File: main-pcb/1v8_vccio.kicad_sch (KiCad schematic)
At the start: 1 part, among them U1 XC7S100-1FGGA484C

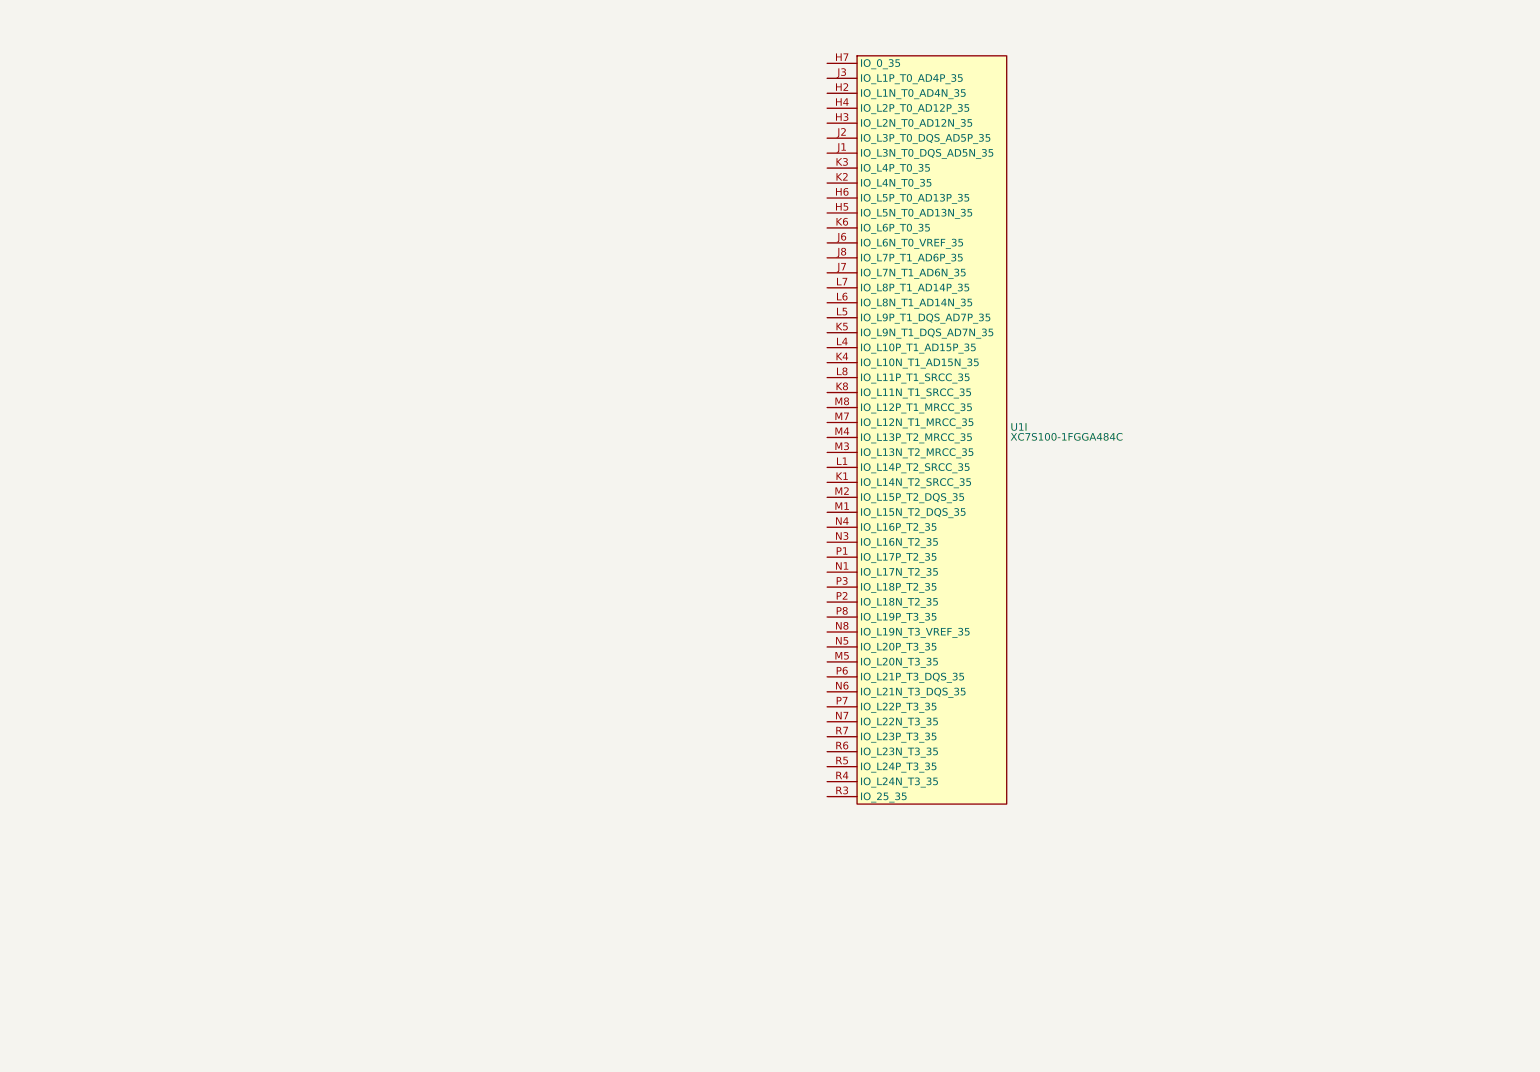
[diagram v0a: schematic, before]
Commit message: Initial design mostly done aside from USB connector, review, test points
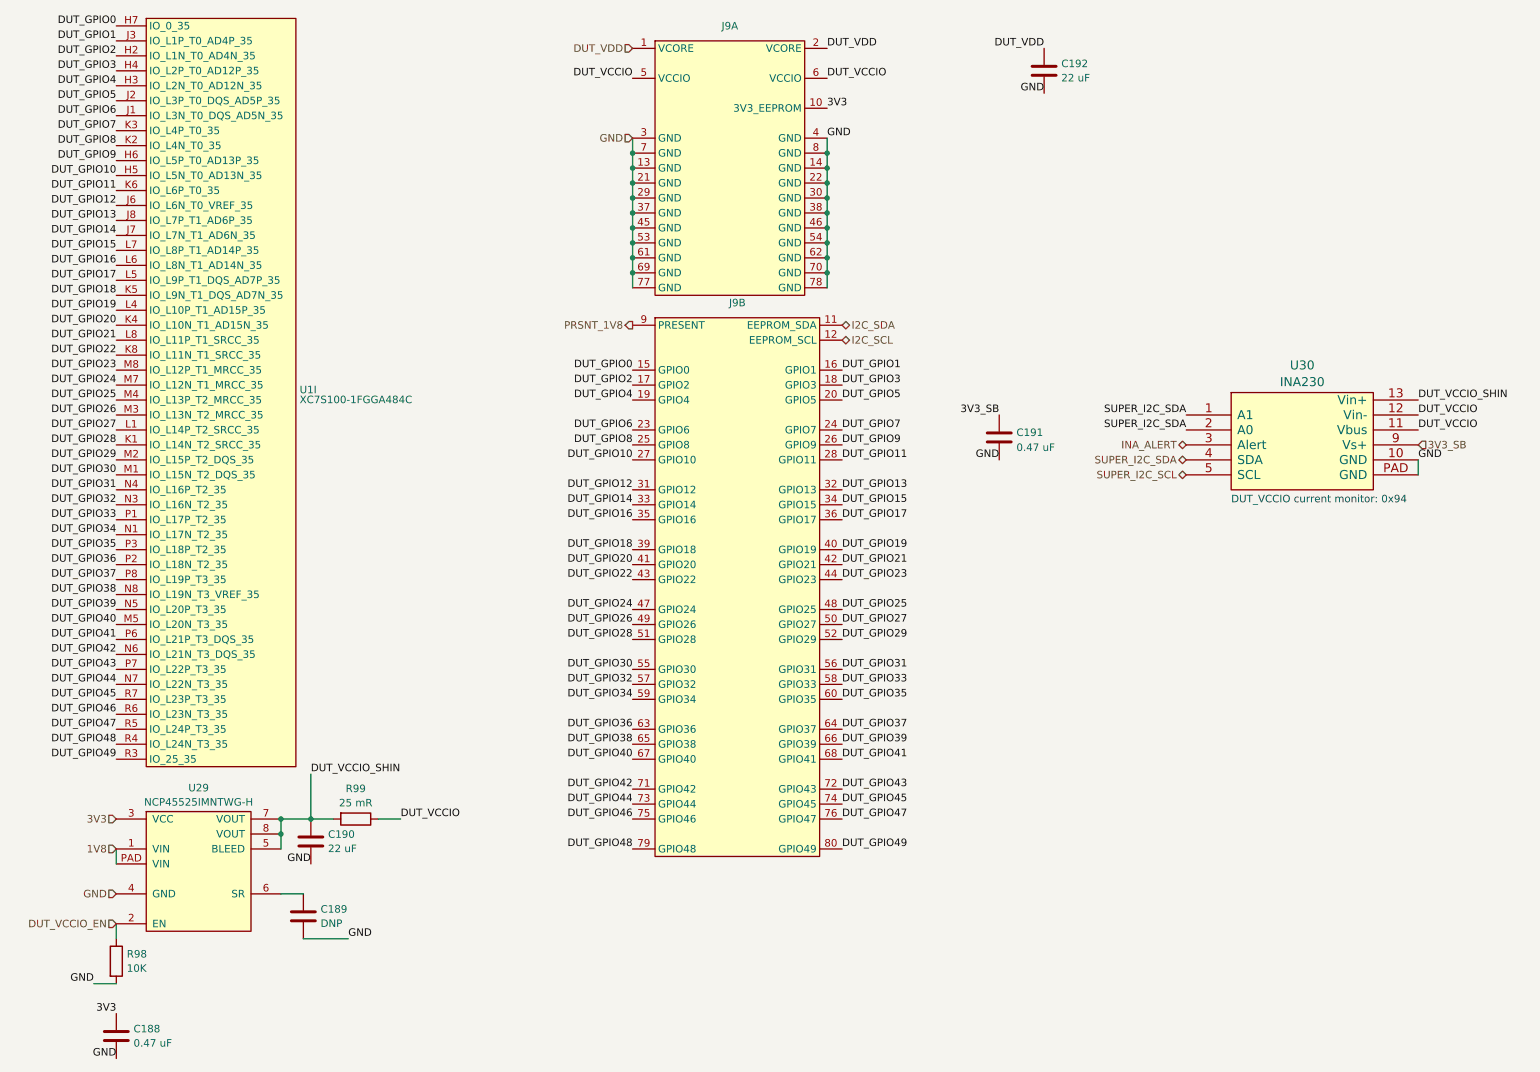
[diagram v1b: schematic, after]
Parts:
- added C188: 0.47 uF, symbol device:C
- added C189: DNP, symbol device:C
- added C190, C192: 22 uF, symbol device:C
- added C191: 0.47 uF, azonenberg_pcb:EIA_0402_CAP_NOSILK, symbol device:C
- added J9: ~, symbol special-azonenberg:CONN_DUMPTRUCK_HOST
- added R98: 10K, symbol device:R
- added R99: 25 mR, symbol passive-azonenberg:R_PWR
- added U29: NCP45525IMNTWG-H, symbol power-azonenberg:NCP45525
- added U30: INA230, azonenberg_pcb:QFN_16_0.5MM_3x3MM, symbol special-azonenberg:INA230
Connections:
- net DUT_GPIO2: now reaches U1.H2 (IO_L1N_T0_AD4N_35)
- net DUT_GPIO2: now also J9.17 (GPIO2)
- net DUT_GPIO4: now reaches U1.H3 (IO_L2N_T0_AD12N_35)
- net DUT_GPIO4: now also J9.19 (GPIO4)
- net DUT_GPIO3: now reaches U1.H4 (IO_L2P_T0_AD12P_35)
- net DUT_GPIO3: now also J9.18 (GPIO3)
- net DUT_GPIO10: now reaches U1.H5 (IO_L5N_T0_AD13N_35)
- net DUT_GPIO10: now also J9.27 (GPIO10)
- net DUT_GPIO9: now reaches U1.H6 (IO_L5P_T0_AD13P_35)
- net DUT_GPIO9: now also J9.26 (GPIO9)
- net DUT_GPIO0: now reaches U1.H7 (IO_0_35)
- net DUT_GPIO0: now also J9.15 (GPIO0)
- net DUT_GPIO6: now reaches U1.J1 (IO_L3N_T0_DQS_AD5N_35)
- net DUT_GPIO6: now also J9.23 (GPIO6)
- net DUT_GPIO5: now reaches U1.J2 (IO_L3P_T0_DQS_AD5P_35)
- net DUT_GPIO5: now also J9.20 (GPIO5)
- net DUT_GPIO1: now reaches U1.J3 (IO_L1P_T0_AD4P_35)
- net DUT_GPIO1: now also J9.16 (GPIO1)
- net DUT_GPIO12: now reaches U1.J6 (IO_L6N_T0_VREF_35)
- net DUT_GPIO12: now also J9.31 (GPIO12)
- net DUT_GPIO14: now reaches U1.J7 (IO_L7N_T1_AD6N_35)
- net DUT_GPIO14: now also J9.33 (GPIO14)
- net DUT_GPIO13: now reaches U1.J8 (IO_L7P_T1_AD6P_35)
- net DUT_GPIO13: now also J9.32 (GPIO13)
- net DUT_GPIO28: now reaches U1.K1 (IO_L14N_T2_SRCC_35)
- net DUT_GPIO28: now also J9.51 (GPIO28)
- net DUT_GPIO8: now reaches U1.K2 (IO_L4N_T0_35)
- net DUT_GPIO8: now also J9.25 (GPIO8)
- net DUT_GPIO7: now reaches U1.K3 (IO_L4P_T0_35)
- net DUT_GPIO7: now also J9.24 (GPIO7)
- net DUT_GPIO20: now reaches U1.K4 (IO_L10N_T1_AD15N_35)
- net DUT_GPIO20: now also J9.41 (GPIO20)
- net DUT_GPIO18: now reaches U1.K5 (IO_L9N_T1_DQS_AD7N_35)
- net DUT_GPIO18: now also J9.39 (GPIO18)
- net DUT_GPIO11: now reaches U1.K6 (IO_L6P_T0_35)
- net DUT_GPIO11: now also J9.28 (GPIO11)
- net DUT_GPIO22: now reaches U1.K8 (IO_L11N_T1_SRCC_35)
- net DUT_GPIO22: now also J9.43 (GPIO22)
- net DUT_GPIO27: now reaches U1.L1 (IO_L14P_T2_SRCC_35)
- net DUT_GPIO27: now also J9.50 (GPIO27)
- net DUT_GPIO19: now reaches U1.L4 (IO_L10P_T1_AD15P_35)
- net DUT_GPIO19: now also J9.40 (GPIO19)
- net DUT_GPIO17: now reaches U1.L5 (IO_L9P_T1_DQS_AD7P_35)
- net DUT_GPIO17: now also J9.36 (GPIO17)
- net DUT_GPIO16: now reaches U1.L6 (IO_L8N_T1_AD14N_35)
- net DUT_GPIO16: now also J9.35 (GPIO16)
- net DUT_GPIO15: now reaches U1.L7 (IO_L8P_T1_AD14P_35)
- net DUT_GPIO15: now also J9.34 (GPIO15)
- net DUT_GPIO21: now reaches U1.L8 (IO_L11P_T1_SRCC_35)
- net DUT_GPIO21: now also J9.42 (GPIO21)
- net DUT_GPIO30: now reaches U1.M1 (IO_L15N_T2_DQS_35)
- net DUT_GPIO30: now also J9.55 (GPIO30)
- net DUT_GPIO29: now reaches U1.M2 (IO_L15P_T2_DQS_35)
- net DUT_GPIO29: now also J9.52 (GPIO29)
- net DUT_GPIO26: now reaches U1.M3 (IO_L13N_T2_MRCC_35)
- net DUT_GPIO26: now also J9.49 (GPIO26)
- net DUT_GPIO25: now reaches U1.M4 (IO_L13P_T2_MRCC_35)
- net DUT_GPIO25: now also J9.48 (GPIO25)
- net DUT_GPIO40: now reaches U1.M5 (IO_L20N_T3_35)
- net DUT_GPIO40: now also J9.67 (GPIO40)
- net DUT_GPIO24: now reaches U1.M7 (IO_L12N_T1_MRCC_35)
- net DUT_GPIO24: now also J9.47 (GPIO24)
- net DUT_GPIO23: now reaches U1.M8 (IO_L12P_T1_MRCC_35)
- net DUT_GPIO23: now also J9.44 (GPIO23)
- net DUT_GPIO34: now reaches U1.N1 (IO_L17N_T2_35)
- net DUT_GPIO34: now also J9.59 (GPIO34)
- net DUT_GPIO32: now reaches U1.N3 (IO_L16N_T2_35)
- net DUT_GPIO32: now also J9.57 (GPIO32)
- net DUT_GPIO31: now reaches U1.N4 (IO_L16P_T2_35)
- net DUT_GPIO31: now also J9.56 (GPIO31)
- net DUT_GPIO39: now reaches U1.N5 (IO_L20P_T3_35)
- net DUT_GPIO39: now also J9.66 (GPIO39)
- net DUT_GPIO42: now reaches U1.N6 (IO_L21N_T3_DQS_35)
- net DUT_GPIO42: now also J9.71 (GPIO42)
- net DUT_GPIO44: now reaches U1.N7 (IO_L22N_T3_35)
- net DUT_GPIO44: now also J9.73 (GPIO44)
- net DUT_GPIO38: now reaches U1.N8 (IO_L19N_T3_VREF_35)
- net DUT_GPIO38: now also J9.65 (GPIO38)
- net DUT_GPIO33: now reaches U1.P1 (IO_L17P_T2_35)
- net DUT_GPIO33: now also J9.58 (GPIO33)
- net DUT_GPIO36: now reaches U1.P2 (IO_L18N_T2_35)
- net DUT_GPIO36: now also J9.63 (GPIO36)
- net DUT_GPIO35: now reaches U1.P3 (IO_L18P_T2_35)
- net DUT_GPIO35: now also J9.60 (GPIO35)
- net DUT_GPIO41: now reaches U1.P6 (IO_L21P_T3_DQS_35)
- net DUT_GPIO41: now also J9.68 (GPIO41)
- net DUT_GPIO43: now reaches U1.P7 (IO_L22P_T3_35)
- net DUT_GPIO43: now also J9.72 (GPIO43)
- net DUT_GPIO37: now reaches U1.P8 (IO_L19P_T3_35)
- net DUT_GPIO37: now also J9.64 (GPIO37)
- net DUT_GPIO49: now reaches U1.R3 (IO_25_35)
- net DUT_GPIO49: now also J9.80 (GPIO49)
- net DUT_GPIO48: now reaches U1.R4 (IO_L24N_T3_35)
- net DUT_GPIO48: now also J9.79 (GPIO48)
- net DUT_GPIO47: now reaches U1.R5 (IO_L24P_T3_35)
- net DUT_GPIO47: now also J9.76 (GPIO47)
- net DUT_GPIO46: now reaches U1.R6 (IO_L23N_T3_35)
- net DUT_GPIO46: now also J9.75 (GPIO46)
- net DUT_GPIO45: now reaches U1.R7 (IO_L23P_T3_35)
- net DUT_GPIO45: now also J9.74 (GPIO45)
- new net: C189.1, U29.6 (SR)
- new net 1V8: U29.1 (VIN), U29.PAD (VIN)
- new net 3V3: C188.1, J9.10 (3V3_EEPROM), U29.3 (VCC)
- new net 3V3_SB: C191.1, U30.9 (Vs+)
- new net DUT_VCCIO: J9.5 (VCCIO), J9.6 (VCCIO), R99.1, U30.11 (Vbus), U30.12 (Vin-)
- new net DUT_VCCIO_EN: R98.1, U29.2 (EN)
- new net DUT_VCCIO_SHIN: C190.1, R99.2, U29.5 (BLEED), U29.7 (VOUT), U29.8 (VOUT), U30.13 (Vin+)
- new net DUT_VDD: C192.1, J9.1 (VCORE), J9.2 (VCORE)
- new net GND: C188.2, C189.2, C190.2, C191.2, C192.2, J9.13 (GND), J9.14 (GND), J9.21 (GND), J9.22 (GND), J9.29 (GND), J9.3 (GND), J9.30 (GND), J9.37 (GND), J9.38 (GND), J9.4 (GND), J9.45 (GND), J9.46 (GND), J9.53 (GND), J9.54 (GND), J9.61 (GND), J9.62 (GND), J9.69 (GND), J9.7 (GND), J9.70 (GND), J9.77 (GND), J9.78 (GND), J9.8 (GND), R98.2, U29.4 (GND), U30.10 (GND), U30.PAD (GND)
- new net I2C_SCL: J9.12 (EEPROM_SCL)
- new net I2C_SDA: J9.11 (EEPROM_SDA)
- new net INA_ALERT: U30.3 (Alert)
- new net PRSNT_1V8: J9.9 (PRESENT)
- new net SUPER_I2C_SCL: U30.5 (SCL)
- new net SUPER_I2C_SDA: U30.1 (A1), U30.2 (A0), U30.4 (SDA)
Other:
- note added: "DUT_VCCIO current monitor: 0x94"
- moved on the sheet: U1I

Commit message: More schematic tweaks and test points
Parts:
- C188, C189: footprint (none) -> azonenberg_pcb:EIA_0402_CAP_NOSILK
- J9: value ~ -> CONN_DUMPTRUCK_HOST
- R98, R99: footprint (none) -> azonenberg_pcb:EIA_0402_RES_NOSILK
- U29: footprint (none) -> azonenberg_pcb:DFN_8_0.5MM_2x2MM
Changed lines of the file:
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@@
 			)
 		)
-		(property "Value" "~"
+		(property "Value" "CONN_DUMPTRUCK_HOST"
 			(at 151.13 20.7399 0)
 			(effects
@@
 			)
 		)
-		(property "Footprint" ""
+		(property "Footprint" "azonenberg_pcb:EIA_0402_RES_NOSILK"
 			(at 87.63 151.892 90)
 			(effects
@@
 			)
 		)
-		(property "Footprint" ""
+		(property "Footprint" "azonenberg_pcb:EIA_0402_CAP_NOSILK"
 			(at 47.9552 194.31 0)
 			(effects
@@
 			)
 		)
-		(property "Footprint" ""
+		(property "Footprint" "azonenberg_pcb:DFN_8_0.5MM_2x2MM"
 			(at 52.07 172.72 0)
 			(effects
@@
 			)
 		)
-		(property "Footprint" ""
+		(property "Footprint" "azonenberg_pcb:EIA_0402_RES_NOSILK"
 			(at 45.212 177.8 90)
 			(effects
@@
 			)
 		)
-		(property "Footprint" ""
+		(property "Footprint" "azonenberg_pcb:EIA_0402_CAP_NOSILK"
 			(at 79.7052 173.99 0)
 			(effects
@@
 			)
 		)
-		(property "Value" "~"
+		(property "Value" "CONN_DUMPTRUCK_HOST"
 			(at 152.4 67.7299 0)
 			(effects

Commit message: Added some RGB LEDs, changed a few voltage dividers to match what was in stock. Time for next round of review.
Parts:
- C190: footprint (none) -> azonenberg_pcb:EIA_0805_CAP_NOSILK
- C192: footprint (none) -> azonenberg_pcb:EIA_1206_CAP_NOSILK
- J9: footprint (none) -> azonenberg_pcb:CONN_SAMTEC_BTE-040-01-F-D-A-K
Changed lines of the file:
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@@
 	(title_block
 		(title "DUMPTRUCK flash dumper")
-		(date "2024-10-16")
+		(date "2024-10-17")
 		(rev "0.1")
 		(company "Antikernel Labs")
@@
 			)
 		)
-		(property "Footprint" ""
+		(property "Footprint" "azonenberg_pcb:CONN_SAMTEC_BTE-040-01-F-D-A-K"
 			(at 138.43 64.77 0)
 			(effects
@@
 			)
 		)
-		(property "Footprint" ""
+		(property "Footprint" "azonenberg_pcb:EIA_0805_CAP_NOSILK"
 			(at 80.9752 161.29 0)
 			(effects
@@
 			)
 		)
-		(property "Footprint" ""
+		(property "Footprint" "azonenberg_pcb:EIA_1206_CAP_NOSILK"
 			(at 205.4352 30.48 0)
 			(effects
@@
 			)
 		)
-		(property "Footprint" ""
+		(property "Footprint" "azonenberg_pcb:CONN_SAMTEC_BTE-040-01-F-D-A-K"
 			(at 138.43 160.02 0)
 			(effects

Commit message: Finished schematic review
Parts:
- R98: value 10K -> DNP
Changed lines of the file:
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@@
 			)
 		)
-		(property "Value" "10K"
+		(property "Value" "DNP"
 			(at 48.768 179.0121 0)
 			(effects
